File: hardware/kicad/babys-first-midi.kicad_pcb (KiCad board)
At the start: 2 copper layers, 100 x 70 mm, 26 parts, among them J1 BFM:RJ45_THT, J2 Connector_Audio:TRS_3.5mm_Hor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, Q1 Package_TO_SOT_THT:TO-220-3_V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, Q2 Package_TO_SOT_THT:TO-220-3_V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, Q3 Package_TO_SOT_THT:TO-220-3_V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, Q4 Package_TO_SOT_THT:TO-220-3_V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, Q5 Package_TO_SOT_THT:TO-220-3_V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, U1 BFM:Pimoroni_Tiny2350_Module

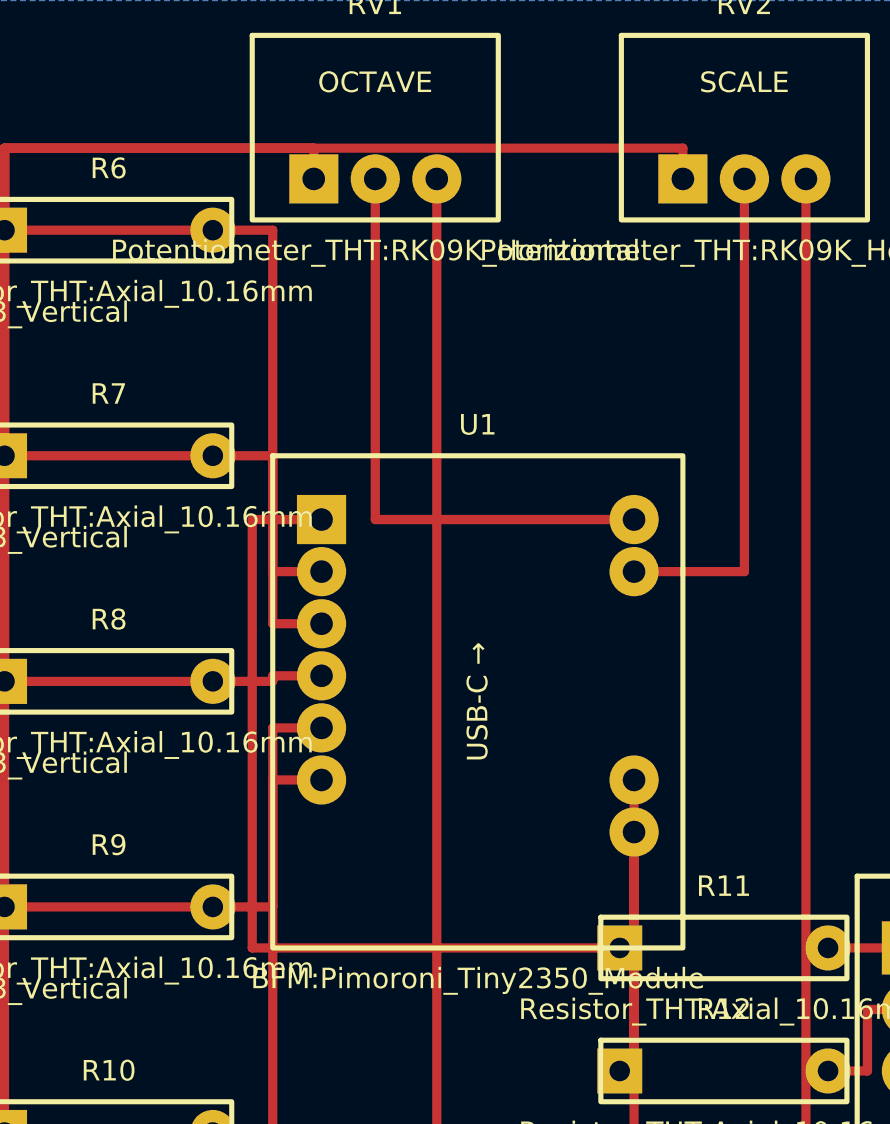
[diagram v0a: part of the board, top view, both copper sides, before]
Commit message: Use full 16-pin Tiny 2350 socket footprint
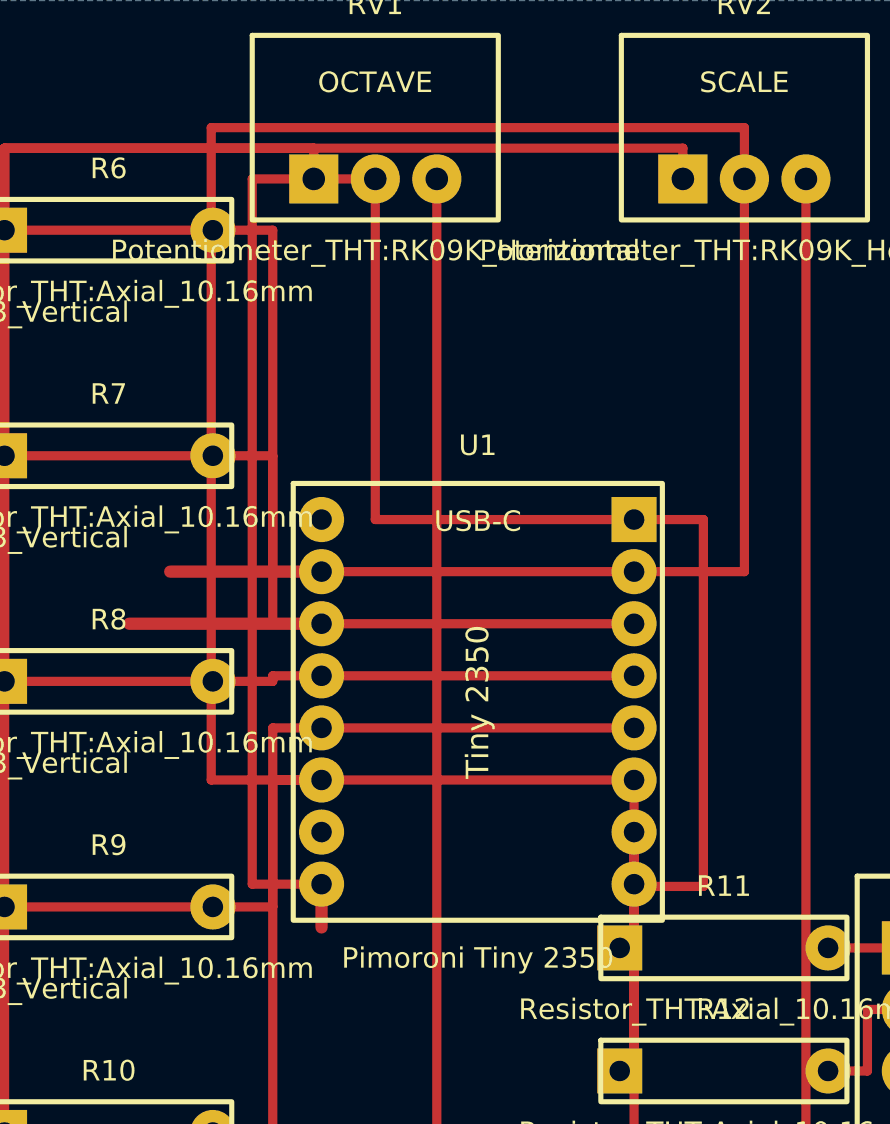
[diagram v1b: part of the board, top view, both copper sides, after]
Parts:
- U1: value BFM:Pimoroni_Tiny2350_Module -> Pimoroni Tiny 2350; footprint BFM:Pimoroni_Tiny2350_Module -> BFM:Pimoroni_Tiny2350_2x8_Header
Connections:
- U1 pad 7: ADC_OCTAVE -> (no net)
- U1 pad 8: ADC_SCALE -> (no net)
- U1 pad 9: 3V3 -> (no net)
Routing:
- net ADC_SCALE: track 24.5 -> 90.2 mm
- net ADC_OCTAVE: track 29.2 -> 73.0 mm
- net MIDI_TX: track 42.2 -> 25.3 mm
- net KEY_G: track 40.6 -> 55.8 mm
- net KEY_F: track 32.1 -> 47.4 mm
- net KEY_E: track 23.6 -> 38.9 mm
- net KEY_D: track 31.6 -> 46.8 mm
- net KEY_C: track 40.0 -> 55.3 mm
- net GND: track 301.7 -> 311.2 mm
- net 3V3: track 196.0 -> 205.4 mm
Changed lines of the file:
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@@
     (pad "2" thru_hole circle (at 5.08 0) (size 2.2 2.2) (drill 1) (layers "*.Cu" "*.Mask") (net 18 "KEY_G"))
   )
-  (footprint "BFM:Pimoroni_Tiny2350_Module" (layer "F.Cu") (at 89 55)
-    (property "Reference" "U1" (at 0 -13.5 0) (layer "F.SilkS") (effects (font (size 1 1) (thickness 0.15))))
-    (property "Value" "BFM:Pimoroni_Tiny2350_Module" (at 0 13.5 0) (layer "F.SilkS") (effects (font (size 1 1) (thickness 0.15))))
-    (fp_rect (start -10 -12) (end 10 12) (stroke (width 0.25) (type default)) (fill none) (layer "F.SilkS"))
-    (pad "1" thru_hole rect (at -7.62 -8.89) (size 2.4 2.4) (drill 1.1) (layers "*.Cu" "*.Mask") (net 19 "MIDI_TX"))
-    (pad "2" thru_hole circle (at -7.62 -6.35) (size 2.4 2.4) (drill 1.1) (layers "*.Cu" "*.Mask") (net 14 "KEY_C"))
-    (pad "3" thru_hole circle (at -7.62 -3.81) (size 2.4 2.4) (drill 1.1) (layers "*.Cu" "*.Mask") (net 15 "KEY_D"))
-    (pad "4" thru_hole circle (at -7.62 -1.27) (size 2.4 2.4) (drill 1.1) (layers "*.Cu" "*.Mask") (net 16 "KEY_E"))
-    (pad "5" thru_hole circle (at -7.62 1.27) (size 2.4 2.4) (drill 1.1) (layers "*.Cu" "*.Mask") (net 17 "KEY_F"))
-    (pad "6" thru_hole circle (at -7.62 3.81) (size 2.4 2.4) (drill 1.1) (layers "*.Cu" "*.Mask") (net 18 "KEY_G"))
-    (pad "7" thru_hole circle (at 7.62 -8.89) (size 2.4 2.4) (drill 1.1) (layers "*.Cu" "*.Mask") (net 20 "ADC_OCTAVE"))
-    (pad "8" thru_hole circle (at 7.62 -6.35) (size 2.4 2.4) (drill 1.1) (layers "*.Cu" "*.Mask") (net 21 "ADC_SCALE"))
-    (pad "9" thru_hole circle (at 7.62 3.81) (size 2.4 2.4) (drill 1.1) (layers "*.Cu" "*.Mask") (net 2 "3V3"))
-    (pad "10" thru_hole circle (at 7.62 6.35) (size 2.4 2.4) (drill 1.1) (layers "*.Cu" "*.Mask") (net 1 "GND"))
-    (fp_text user "USB-C →" (at 0 0 90) (layer "F.SilkS") (effects (font (size 1 1) (thickness 0.15))))
+  (footprint "BFM:Pimoroni_Tiny2350_2x8_Header" (layer "F.Cu") (at 89 55)
+    (property "Reference" "U1" (at 0 -12.5 0) (layer "F.SilkS") (effects (font (size 1 1) (thickness 0.15))))
+    (property "Value" "Pimoroni Tiny 2350" (at 0 12.5 0) (layer "F.SilkS") (effects (font (size 1 1) (thickness 0.15))))
+    (fp_rect (start -9 -10.65) (end 9 10.65) (stroke (width 0.25) (type default)) (fill none) (layer "F.SilkS"))
+    (fp_text user "USB-C" (at 0 -8.8 0) (layer "F.SilkS") (effects (font (size 1 1) (thickness 0.15))))
+    (fp_text user "Tiny 2350" (at 0 0 90) (layer "F.SilkS") (effects (font (size 1.1 1.1) (thickness 0.15))))
+    (pad "1" thru_hole rect (at 7.62 -8.89) (size 2.2 2.2) (drill 1.0) (layers "*.Cu" "*.Mask") (net 19 "MIDI_TX"))
+    (pad "2" thru_hole circle (at 7.62 -6.35) (size 2.2 2.2) (drill 1.0) (layers "*.Cu" "*.Mask") (net 14 "KEY_C"))
+    (pad "3" thru_hole circle (at 7.62 -3.81) (size 2.2 2.2) (drill 1.0) (layers "*.Cu" "*.Mask") (net 15 "KEY_D"))
+    (pad "4" thru_hole circle (at 7.62 -1.27) (size 2.2 2.2) (drill 1.0) (layers "*.Cu" "*.Mask") (net 16 "KEY_E"))
+    (pad "5" thru_hole circle (at 7.62 1.27) (size 2.2 2.2) (drill 1.0) (layers "*.Cu" "*.Mask") (net 17 "KEY_F"))
+    (pad "6" thru_hole circle (at 7.62 3.81) (size 2.2 2.2) (drill 1.0) (layers "*.Cu" "*.Mask") (net 18 "KEY_G"))
+    (pad "7" thru_hole circle (at 7.62 6.35) (size 2.2 2.2) (drill 1.0) (layers "*.Cu" "*.Mask"))
+    (pad "8" thru_hole circle (at 7.62 8.89) (size 2.2 2.2) (drill 1.0) (layers "*.Cu" "*.Mask"))
+    (pad "9" thru_hole circle (at -7.62 -8.89) (size 2.2 2.2) (drill 1.0) (layers "*.Cu" "*.Mask"))
+    (pad "10" thru_hole circle (at -7.62 -6.35) (size 2.2 2.2) (drill 1.0) (layers "*.Cu" "*.Mask") (net 1 "GND"))
+    (pad "11" thru_hole circle (at -7.62 -3.81) (size 2.2 2.2) (drill 1.0) (layers "*.Cu" "*.Mask") (net 2 "3V3"))
+    (pad "12" thru_hole circle (at -7.62 -1.27) (size 2.2 2.2) (drill 1.0) (layers "*.Cu" "*.Mask"))
+    (pad "13" thru_hole circle (at -7.62 1.27) (size 2.2 2.2) (drill 1.0) (layers "*.Cu" "*.Mask"))
+    (pad "14" thru_hole circle (at -7.62 3.81) (size 2.2 2.2) (drill 1.0) (layers "*.Cu" "*.Mask") (net 21 "ADC_SCALE"))
+    (pad "15" thru_hole circle (at -7.62 6.35) (size 2.2 2.2) (drill 1.0) (layers "*.Cu" "*.Mask") (net 20 "ADC_OCTAVE"))
+    (pad "16" thru_hole circle (at -7.62 8.89) (size 2.2 2.2) (drill 1.0) (layers "*.Cu" "*.Mask") (net 1 "GND"))
   )
   (footprint "Potentiometer_THT:RK09K_Horizontal" (layer "F.Cu") (at 84 27)
@@
   (segment (start 76.08 32) (end 79 32) (width 0.45) (layer "F.Cu") (net 14))
   (segment (start 79 32) (end 79 48.65) (width 0.45) (layer "F.Cu") (net 14))
-  (segment (start 79 48.65) (end 81.38 48.65) (width 0.45) (layer "F.Cu") (net 14))
+  (segment (start 79 48.65) (end 96.62 48.65) (width 0.45) (layer "F.Cu") (net 14))
   (segment (start 76.08 43) (end 79 43) (width 0.45) (layer "F.Cu") (net 15))
   (segment (start 79 43) (end 79 51.19) (width 0.45) (layer "F.Cu") (net 15))
-  (segment (start 79 51.19) (end 81.38 51.19) (width 0.45) (layer "F.Cu") (net 15))
+  (segment (start 79 51.19) (end 96.62 51.19) (width 0.45) (layer "F.Cu") (net 15))
   (segment (start 76.08 54) (end 79 54) (width 0.45) (layer "F.Cu") (net 16))
   (segment (start 79 54) (end 79 53.73) (width 0.45) (layer "F.Cu") (net 16))
-  (segment (start 79 53.73) (end 81.38 53.73) (width 0.45) (layer "F.Cu") (net 16))
+  (segment (start 79 53.73) (end 96.62 53.73) (width 0.45) (layer "F.Cu") (net 16))
   (segment (start 76.08 65) (end 79 65) (width 0.45) (layer "F.Cu") (net 17))
   (segment (start 79 65) (end 79 56.27) (width 0.45) (layer "F.Cu") (net 17))
-  (segment (start 79 56.27) (end 81.38 56.27) (width 0.45) (layer "F.Cu") (net 17))
+  (segment (start 79 56.27) (end 96.62 56.27) (width 0.45) (layer "F.Cu") (net 17))
   (segment (start 76.08 76) (end 79 76) (width 0.45) (layer "F.Cu") (net 18))
   (segment (start 79 76) (end 79 58.81) (width 0.45) (layer "F.Cu") (net 18))
-  (segment (start 79 58.81) (end 81.38 58.81) (width 0.45) (layer "F.Cu") (net 18))
-  (segment (start 81.38 46.11) (end 78 46.11) (width 0.45) (layer "F.Cu") (net 19))
-  (segment (start 78 46.11) (end 78 67) (width 0.45) (layer "F.Cu") (net 19))
-  (segment (start 78 67) (end 95.92 67) (width 0.45) (layer "F.Cu") (net 19))
+  (segment (start 79 58.81) (end 96.62 58.81) (width 0.45) (layer "F.Cu") (net 18))
+  (segment (start 96.62 46.11) (end 100 46.11) (width 0.45) (layer "F.Cu") (net 19))
+  (segment (start 100 46.11) (end 100 64) (width 0.45) (layer "F.Cu") (net 19))
+  (segment (start 100 64) (end 95.92 64) (width 0.45) (layer "F.Cu") (net 19))
   (segment (start 96.62 46.11) (end 84 46.11) (width 0.45) (layer "F.Cu") (net 20))
   (segment (start 84 46.11) (end 84 29.5) (width 0.45) (layer "F.Cu") (net 20))
@@
   (segment (start 108 73) (end 108 70) (width 0.45) (layer "F.Cu") (net 23))
   (segment (start 108 70) (end 110 70) (width 0.45) (layer "F.Cu") (net 23))
+  (segment (start 81.38 63.89) (end 78 63.89) (width 0.45) (layer "F.Cu") (net 20))
+  (segment (start 78 63.89) (end 78 29.5) (width 0.45) (layer "F.Cu") (net 20))
+  (segment (start 78 29.5) (end 84 29.5) (width 0.45) (layer "F.Cu") (net 20))
+  (segment (start 81.38 58.81) (end 76 58.81) (width 0.45) (layer "F.Cu") (net 21))
+  (segment (start 76 58.81) (end 76 27) (width 0.45) (layer "F.Cu") (net 21))
+  (segment (start 76 27) (end 102 27) (width 0.45) (layer "F.Cu") (net 21))
+  (segment (start 102 27) (end 102 29.5) (width 0.45) (layer "F.Cu") (net 21))
+  (segment (start 81.38 51.19) (end 72 51.19) (width 0.6) (layer "F.Cu") (net 2))
+  (segment (start 81.38 48.65) (end 74 48.65) (width 0.6) (layer "F.Cu") (net 1))
+  (segment (start 81.38 63.89) (end 81.38 66) (width 0.6) (layer "F.Cu") (net 1))
   (zone (net 1) (net_name "GND") (layer "B.Cu") (hatch edge 0.5)
     (connect_pads (clearance 0.5))

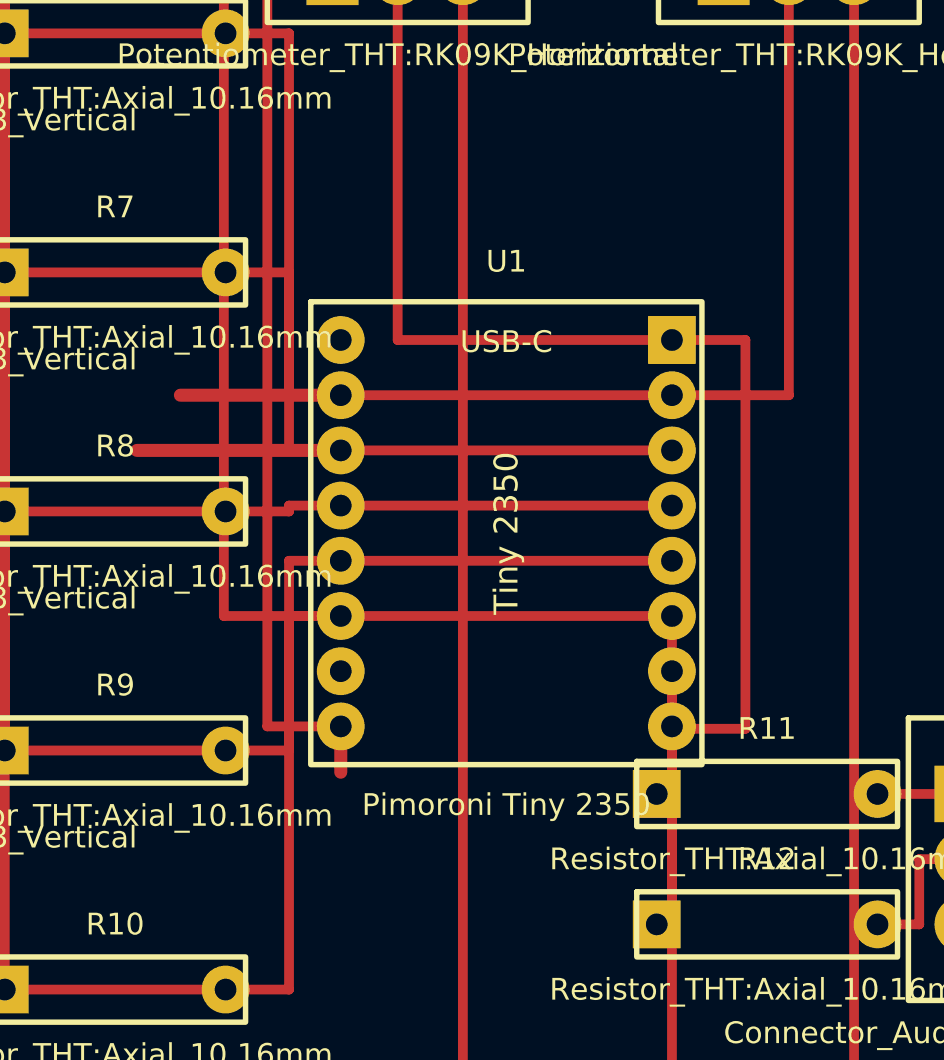
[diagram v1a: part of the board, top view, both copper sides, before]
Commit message: Move Tiny 2350 for resistor clearance
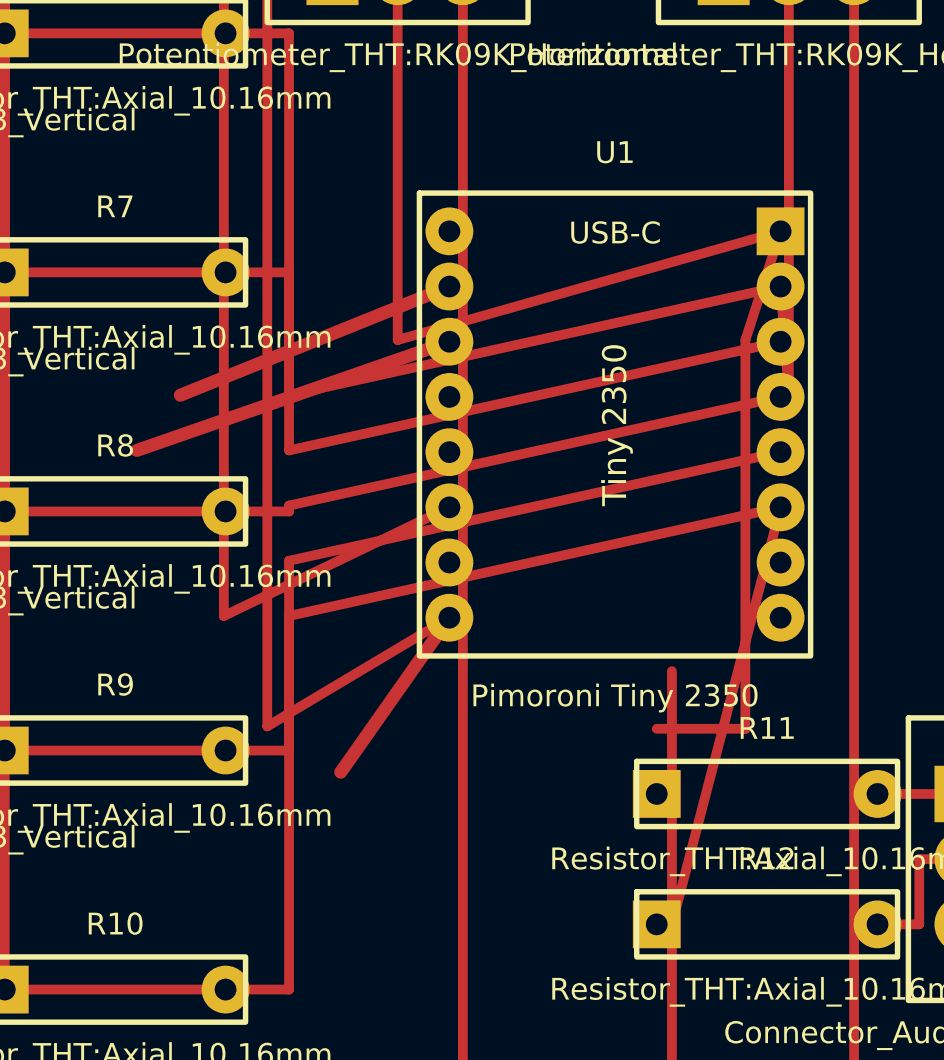
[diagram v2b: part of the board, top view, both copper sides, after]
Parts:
- moved U1 7.07 mm to (94.0, 50.0)
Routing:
- net GND: track 311.2 -> 323.8 mm
- net ADC_OCTAVE: track 73.0 -> 85.1 mm
- net 3V3: track 205.4 -> 216.9 mm
- net ADC_SCALE: track 90.2 -> 96.0 mm
- net KEY_G: track 55.8 -> 61.4 mm
- net KEY_F: track 47.4 -> 52.9 mm
- net KEY_E: track 38.9 -> 44.4 mm
- net KEY_D: track 46.8 -> 52.4 mm
- net KEY_C: track 55.3 -> 60.8 mm
- net MIDI_TX: track 25.3 -> 27.2 mm
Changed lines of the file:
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@@
     (pad "2" thru_hole circle (at 5.08 0) (size 2.2 2.2) (drill 1) (layers "*.Cu" "*.Mask") (net 18 "KEY_G"))
   )
-  (footprint "BFM:Pimoroni_Tiny2350_2x8_Header" (layer "F.Cu") (at 89 55)
+  (footprint "BFM:Pimoroni_Tiny2350_2x8_Header" (layer "F.Cu") (at 94 50)
     (property "Reference" "U1" (at 0 -12.5 0) (layer "F.SilkS") (effects (font (size 1 1) (thickness 0.15))))
     (property "Value" "Pimoroni Tiny 2350" (at 0 12.5 0) (layer "F.SilkS") (effects (font (size 1 1) (thickness 0.15))))
@@
   (segment (start 81 29.5) (end 81 28) (width 0.45) (layer "F.Cu") (net 2))
   (segment (start 81 28) (end 65.92 28) (width 0.45) (layer "F.Cu") (net 2))
-  (segment (start 96.62 58.81) (end 96.62 73) (width 0.45) (layer "F.Cu") (net 2))
+  (segment (start 101.62 53.81) (end 96.62 73) (width 0.45) (layer "F.Cu") (net 2))
   (segment (start 96.62 73) (end 95.92 73) (width 0.45) (layer "F.Cu") (net 2))
   (segment (start 60.54 82) (end 96.62 82) (width 0.45) (layer "F.Cu") (net 1))
@@
   (segment (start 76.08 32) (end 79 32) (width 0.45) (layer "F.Cu") (net 14))
   (segment (start 79 32) (end 79 48.65) (width 0.45) (layer "F.Cu") (net 14))
-  (segment (start 79 48.65) (end 96.62 48.65) (width 0.45) (layer "F.Cu") (net 14))
+  (segment (start 79 48.65) (end 101.62 43.65) (width 0.45) (layer "F.Cu") (net 14))
   (segment (start 76.08 43) (end 79 43) (width 0.45) (layer "F.Cu") (net 15))
   (segment (start 79 43) (end 79 51.19) (width 0.45) (layer "F.Cu") (net 15))
-  (segment (start 79 51.19) (end 96.62 51.19) (width 0.45) (layer "F.Cu") (net 15))
+  (segment (start 79 51.19) (end 101.62 46.19) (width 0.45) (layer "F.Cu") (net 15))
   (segment (start 76.08 54) (end 79 54) (width 0.45) (layer "F.Cu") (net 16))
   (segment (start 79 54) (end 79 53.73) (width 0.45) (layer "F.Cu") (net 16))
-  (segment (start 79 53.73) (end 96.62 53.73) (width 0.45) (layer "F.Cu") (net 16))
+  (segment (start 79 53.73) (end 101.62 48.73) (width 0.45) (layer "F.Cu") (net 16))
   (segment (start 76.08 65) (end 79 65) (width 0.45) (layer "F.Cu") (net 17))
   (segment (start 79 65) (end 79 56.27) (width 0.45) (layer "F.Cu") (net 17))
-  (segment (start 79 56.27) (end 96.62 56.27) (width 0.45) (layer "F.Cu") (net 17))
+  (segment (start 79 56.27) (end 101.62 51.27) (width 0.45) (layer "F.Cu") (net 17))
   (segment (start 76.08 76) (end 79 76) (width 0.45) (layer "F.Cu") (net 18))
   (segment (start 79 76) (end 79 58.81) (width 0.45) (layer "F.Cu") (net 18))
-  (segment (start 79 58.81) (end 96.62 58.81) (width 0.45) (layer "F.Cu") (net 18))
-  (segment (start 96.62 46.11) (end 100 46.11) (width 0.45) (layer "F.Cu") (net 19))
+  (segment (start 79 58.81) (end 101.62 53.81) (width 0.45) (layer "F.Cu") (net 18))
+  (segment (start 101.62 41.11) (end 100 46.11) (width 0.45) (layer "F.Cu") (net 19))
   (segment (start 100 46.11) (end 100 64) (width 0.45) (layer "F.Cu") (net 19))
   (segment (start 100 64) (end 95.92 64) (width 0.45) (layer "F.Cu") (net 19))
-  (segment (start 96.62 46.11) (end 84 46.11) (width 0.45) (layer "F.Cu") (net 20))
+  (segment (start 101.62 41.11) (end 84 46.11) (width 0.45) (layer "F.Cu") (net 20))
   (segment (start 84 46.11) (end 84 29.5) (width 0.45) (layer "F.Cu") (net 20))
-  (segment (start 96.62 48.65) (end 102 48.65) (width 0.45) (layer "F.Cu") (net 21))
+  (segment (start 101.62 43.65) (end 102 48.65) (width 0.45) (layer "F.Cu") (net 21))
   (segment (start 102 48.65) (end 102 29.5) (width 0.45) (layer "F.Cu") (net 21))
   (segment (start 106.08 67) (end 110 67) (width 0.45) (layer "F.Cu") (net 22))
@@
   (segment (start 108 73) (end 108 70) (width 0.45) (layer "F.Cu") (net 23))
   (segment (start 108 70) (end 110 70) (width 0.45) (layer "F.Cu") (net 23))
-  (segment (start 81.38 63.89) (end 78 63.89) (width 0.45) (layer "F.Cu") (net 20))
+  (segment (start 86.38 58.89) (end 78 63.89) (width 0.45) (layer "F.Cu") (net 20))
   (segment (start 78 63.89) (end 78 29.5) (width 0.45) (layer "F.Cu") (net 20))
   (segment (start 78 29.5) (end 84 29.5) (width 0.45) (layer "F.Cu") (net 20))
-  (segment (start 81.38 58.81) (end 76 58.81) (width 0.45) (layer "F.Cu") (net 21))
+  (segment (start 86.38 53.81) (end 76 58.81) (width 0.45) (layer "F.Cu") (net 21))
   (segment (start 76 58.81) (end 76 27) (width 0.45) (layer "F.Cu") (net 21))
   (segment (start 76 27) (end 102 27) (width 0.45) (layer "F.Cu") (net 21))
   (segment (start 102 27) (end 102 29.5) (width 0.45) (layer "F.Cu") (net 21))
-  (segment (start 81.38 51.19) (end 72 51.19) (width 0.6) (layer "F.Cu") (net 2))
-  (segment (start 81.38 48.65) (end 74 48.65) (width 0.6) (layer "F.Cu") (net 1))
-  (segment (start 81.38 63.89) (end 81.38 66) (width 0.6) (layer "F.Cu") (net 1))
+  (segment (start 86.38 46.19) (end 72 51.19) (width 0.6) (layer "F.Cu") (net 2))
+  (segment (start 86.38 43.65) (end 74 48.65) (width 0.6) (layer "F.Cu") (net 1))
+  (segment (start 86.38 58.89) (end 81.38 66) (width 0.6) (layer "F.Cu") (net 1))
   (zone (net 1) (net_name "GND") (layer "B.Cu") (hatch edge 0.5)
     (connect_pads (clearance 0.5))
